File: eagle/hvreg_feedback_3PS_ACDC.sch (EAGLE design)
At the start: 35 parts

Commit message: tweaks - submit to advanced circuits
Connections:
- net N$10: now also U$3.-VOUT
- net N$5: now also U$3.+VOUT
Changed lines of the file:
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@@
 <grid distance="0.1" unitdist="inch" unit="inch" style="lines" multiple="1" display="no" altdistance="0.01" altunitdist="inch" altunit="inch"/>
 <layers>
-<layer number="1" name="Top" color="4" fill="1" visible="yes" active="no"/>
-<layer number="2" name="Route2" color="1" fill="3" visible="yes" active="no"/>
-<layer number="3" name="Route3" color="4" fill="3" visible="yes" active="no"/>
-<layer number="4" name="Route4" color="1" fill="4" visible="yes" active="no"/>
-<layer number="5" name="Route5" color="4" fill="4" visible="yes" active="no"/>
-<layer number="6" name="Route6" color="1" fill="8" visible="yes" active="no"/>
-<layer number="7" name="Route7" color="4" fill="8" visible="yes" active="no"/>
-<layer number="8" name="Route8" color="1" fill="2" visible="yes" active="no"/>
-<layer number="9" name="Route9" color="4" fill="2" visible="yes" active="no"/>
-<layer number="10" name="Route10" color="1" fill="7" visible="yes" active="no"/>
-<layer number="11" name="Route11" color="4" fill="7" visible="yes" active="no"/>
-<layer number="12" name="Route12" color="1" fill="5" visible="yes" active="no"/>
-<layer number="13" name="Route13" color="4" fill="5" visible="yes" active="no"/>
-<layer number="14" name="Route14" color="1" fill="6" visible="yes" active="no"/>
-<layer number="15" name="Route15" color="4" fill="6" visible="yes" active="no"/>
-<layer number="16" name="Bottom" color="1" fill="1" visible="yes" active="no"/>
-<layer number="17" name="Pads" color="2" fill="1" visible="yes" active="no"/>
-<layer number="18" name="Vias" color="2" fill="1" visible="yes" active="no"/>
-<layer number="19" name="Unrouted" color="6" fill="1" visible="yes" active="no"/>
-<layer number="20" name="Dimension" color="15" fill="1" visible="yes" active="no"/>
-<layer number="21" name="tPlace" color="7" fill="1" visible="yes" active="no"/>
-<layer number="22" name="bPlace" color="7" fill="1" visible="yes" active="no"/>
-<layer number="23" name="tOrigins" color="15" fill="1" visible="yes" active="no"/>
-<layer number="24" name="bOrigins" color="15" fill="1" visible="yes" active="no"/>
-<layer number="25" name="tNames" color="7" fill="1" visible="yes" active="no"/>
-<layer number="26" name="bNames" color="7" fill="1" visible="yes" active="no"/>
-<layer number="27" name="tValues" color="7" fill="1" visible="yes" active="no"/>
-<layer number="28" name="bValues" color="7" fill="1" visible="yes" active="no"/>
+<layer number="1" name="Top" color="4" fill="1" visible="no" active="no"/>
+<layer number="2" name="Route2" color="1" fill="3" visible="no" active="no"/>
+<layer number="3" name="Route3" color="4" fill="3" visible="no" active="no"/>
+<layer number="4" name="Route4" color="1" fill="4" visible="no" active="no"/>
+<layer number="5" name="Route5" color="4" fill="4" visible="no" active="no"/>
+<layer number="6" name="Route6" color="1" fill="8" visible="no" active="no"/>
+<layer number="7" name="Route7" color="4" fill="8" visible="no" active="no"/>
+<layer number="8" name="Route8" color="1" fill="2" visible="no" active="no"/>
+<layer number="9" name="Route9" color="4" fill="2" visible="no" active="no"/>
+<layer number="10" name="Route10" color="1" fill="7" visible="no" active="no"/>
+<layer number="11" name="Route11" color="4" fill="7" visible="no" active="no"/>
+<layer number="12" name="Route12" color="1" fill="5" visible="no" active="no"/>
+<layer number="13" name="Route13" color="4" fill="5" visible="no" active="no"/>
+<layer number="14" name="Route14" color="1" fill="6" visible="no" active="no"/>
+<layer number="15" name="Route15" color="4" fill="6" visible="no" active="no"/>
+<layer number="16" name="Bottom" color="1" fill="1" visible="no" active="no"/>
+<layer number="17" name="Pads" color="2" fill="1" visible="no" active="no"/>
+<layer number="18" name="Vias" color="2" fill="1" visible="no" active="no"/>
+<layer number="19" name="Unrouted" color="6" fill="1" visible="no" active="no"/>
+<layer number="20" name="Dimension" color="15" fill="1" visible="no" active="no"/>
+<layer number="21" name="tPlace" color="7" fill="1" visible="no" active="no"/>
+<layer number="22" name="bPlace" color="7" fill="1" visible="no" active="no"/>
+<layer number="23" name="tOrigins" color="15" fill="1" visible="no" active="no"/>
+<layer number="24" name="bOrigins" color="15" fill="1" visible="no" active="no"/>
+<layer number="25" name="tNames" color="7" fill="1" visible="no" active="no"/>
+<layer number="26" name="bNames" color="7" fill="1" visible="no" active="no"/>
+<layer number="27" name="tValues" color="7" fill="1" visible="no" active="no"/>
+<layer number="28" name="bValues" color="7" fill="1" visible="no" active="no"/>
 <layer number="29" name="tStop" color="7" fill="3" visible="no" active="no"/>
 <layer number="30" name="bStop" color="7" fill="6" visible="no" active="no"/>
@@
 <layer number="35" name="tGlue" color="7" fill="4" visible="no" active="no"/>
 <layer number="36" name="bGlue" color="7" fill="5" visible="no" active="no"/>
-<layer number="37" name="tTest" color="7" fill="1" visible="yes" active="no"/>
-<layer number="38" name="bTest" color="7" fill="1" visible="yes" active="no"/>
+<layer number="37" name="tTest" color="7" fill="1" visible="no" active="no"/>
+<layer number="38" name="bTest" color="7" fill="1" visible="no" active="no"/>
 <layer number="39" name="tKeepout" color="4" fill="11" visible="no" active="no"/>
 <layer number="40" name="bKeepout" color="1" fill="11" visible="no" active="no"/>
@@
 <layer number="44" name="Drills" color="7" fill="1" visible="no" active="no"/>
 <layer number="45" name="Holes" color="7" fill="1" visible="no" active="no"/>
-<layer number="46" name="Milling" color="3" fill="1" visible="yes" active="no"/>
-<layer number="47" name="Measures" color="7" fill="1" visible="yes" active="no"/>
-<layer number="48" name="Document" color="7" fill="1" visible="yes" active="no"/>
-<layer number="49" name="Reference" color="7" fill="1" visible="yes" active="no"/>
-<layer number="50" name="dxf" color="7" fill="1" visible="yes" active="no"/>
-<layer number="51" name="tDocu" color="7" fill="1" visible="yes" active="no"/>
-<layer number="52" name="bDocu" color="7" fill="1" visible="yes" active="no"/>
-<layer number="53" name="tGND_GNDA" color="7" fill="9" visible="yes" active="no"/>
-<layer number="54" name="bGND_GNDA" color="1" fill="9" visible="yes" active="no"/>
-<layer number="56" name="wert" color="7" fill="1" visible="yes" active="no"/>
+<layer number="46" name="Milling" color="3" fill="1" visible="no" active="no"/>
+<layer number="47" name="Measures" color="7" fill="1" visible="no" active="no"/>
+<layer number="48" name="Document" color="7" fill="1" visible="no" active="no"/>
+<layer number="49" name="Reference" color="7" fill="1" visible="no" active="no"/>
+<layer number="50" name="dxf" color="7" fill="1" visible="no" active="no"/>
+<layer number="51" name="tDocu" color="7" fill="1" visible="no" active="no"/>
+<layer number="52" name="bDocu" color="7" fill="1" visible="no" active="no"/>
+<layer number="53" name="tGND_GNDA" color="7" fill="9" visible="no" active="no"/>
+<layer number="54" name="bGND_GNDA" color="1" fill="9" visible="no" active="no"/>
+<layer number="56" name="wert" color="7" fill="1" visible="no" active="no"/>
 <layer number="90" name="Modules" color="5" fill="1" visible="yes" active="yes"/>
 <layer number="91" name="Nets" color="2" fill="1" visible="yes" active="yes"/>
@@
 <wire x1="144.78" y1="50.8" x2="144.78" y2="48.26" width="0.1524" layer="91"/>
 <junction x="144.78" y="48.26"/>
+<pinref part="U$3" gate="G$1" pin="+VOUT"/>
 </segment>
 </net>
@@
 <wire x1="144.78" y1="10.16" x2="144.78" y2="22.86" width="0.1524" layer="91"/>
 <pinref part="D4" gate="1" pin="C"/>
-</segment>
-</net>
+<pinref part="U$3" gate="G$1" pin="-VOUT"/>
+</segment>
+</net>

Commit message: use lm317, appropriate opamp resistor selection, ultra gatedriver stacks 4 fets
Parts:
- added C17, C18, C19: .1u, rcl:C-US102-043X133
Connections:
- net GND: now also C17.2, C18.2, C19.2
- net N$13: now also C17.1
- net N$14: now also C19.1
- net N$15: now also C18.1
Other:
- moved on the sheet: CONTROLHV-3
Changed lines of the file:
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@@
 <part name="CONTROLHV" library="con-molex" deviceset="KK-156-4" device=""/>
 <part name="FDBKHV" library="con-molex" deviceset="KK-156-4" device=""/>
+<part name="C17" library="rcl" deviceset="C-US" device="102-043X133" value=".1u"/>
+<part name="C18" library="rcl" deviceset="C-US" device="102-043X133" value=".1u"/>
+<part name="C19" library="rcl" deviceset="C-US" device="102-043X133" value=".1u"/>
+<part name="GND24" library="supply1" deviceset="GND" device=""/>
+<part name="GND29" library="supply1" deviceset="GND" device=""/>
+<part name="GND30" library="supply1" deviceset="GND" device=""/>
 </parts>
 <sheets>
@@
 <instance part="CONTROLHV" gate="-1" x="17.78" y="53.34" rot="R180"/>
 <instance part="CONTROLHV" gate="-2" x="106.68" y="27.94" rot="R180"/>
-<instance part="CONTROLHV" gate="-3" x="33.02" y="-5.08" rot="R180"/>
+<instance part="CONTROLHV" gate="-3" x="17.78" y="-5.08" rot="R180"/>
 <instance part="CONTROLHV" gate="-4" x="5.08" y="33.02" rot="R90"/>
 <instance part="FDBKHV" gate="-1" x="96.52" y="63.5"/>
@@
 <instance part="FDBKHV" gate="-3" x="101.6" y="-20.32"/>
 <instance part="FDBKHV" gate="-4" x="12.7" y="33.02" rot="R90"/>
+<instance part="C17" gate="G$1" x="22.86" y="50.8"/>
+<instance part="C18" gate="G$1" x="22.86" y="-7.62"/>
+<instance part="C19" gate="G$1" x="109.22" y="25.4"/>
+<instance part="GND24" gate="1" x="22.86" y="43.18"/>
+<instance part="GND29" gate="1" x="109.22" y="17.78"/>
+<instance part="GND30" gate="1" x="22.86" y="-15.24"/>
 </instances>
 <busses>
@@
 <pinref part="FDBKHV" gate="-4" pin="S"/>
 <pinref part="GND15" gate="1" pin="GND"/>
+</segment>
+<segment>
+<pinref part="C17" gate="G$1" pin="2"/>
+<pinref part="GND24" gate="1" pin="GND"/>
+</segment>
+<segment>
+<pinref part="C19" gate="G$1" pin="2"/>
+<pinref part="GND29" gate="1" pin="GND"/>
+</segment>
+<segment>
+<pinref part="C18" gate="G$1" pin="2"/>
+<pinref part="GND30" gate="1" pin="GND"/>
 </segment>
 </net>
@@
 <segment>
 <pinref part="U$1" gate="G$1" pin="+VIN"/>
-<wire x1="20.32" y1="53.34" x2="35.56" y2="53.34" width="0.1524" layer="91"/>
+<wire x1="20.32" y1="53.34" x2="22.86" y2="53.34" width="0.1524" layer="91"/>
 <pinref part="CONTROLHV" gate="-1" pin="S"/>
+<pinref part="C17" gate="G$1" pin="1"/>
+<wire x1="22.86" y1="53.34" x2="35.56" y2="53.34" width="0.1524" layer="91"/>
+<junction x="22.86" y="53.34"/>
 </segment>
 </net>
@@
 <wire x1="109.22" y1="27.94" x2="119.38" y2="27.94" width="0.1524" layer="91"/>
 <pinref part="CONTROLHV" gate="-2" pin="S"/>
+<pinref part="C19" gate="G$1" pin="1"/>
+<junction x="109.22" y="27.94"/>
 </segment>
 </net>
@@
 <pinref part="U$2" gate="G$1" pin="+VIN"/>
 <pinref part="CONTROLHV" gate="-3" pin="S"/>
-</segment>
-</net>
+<wire x1="20.32" y1="-5.08" x2="22.86" y2="-5.08" width="0.1524" layer="91"/>
+<pinref part="C18" gate="G$1" pin="1"/>
+<wire x1="22.86" y1="-5.08" x2="35.56" y2="-5.08" width="0.1524" layer="91"/>
+<junction x="22.86" y="-5.08"/>
+</segment>
+</net>

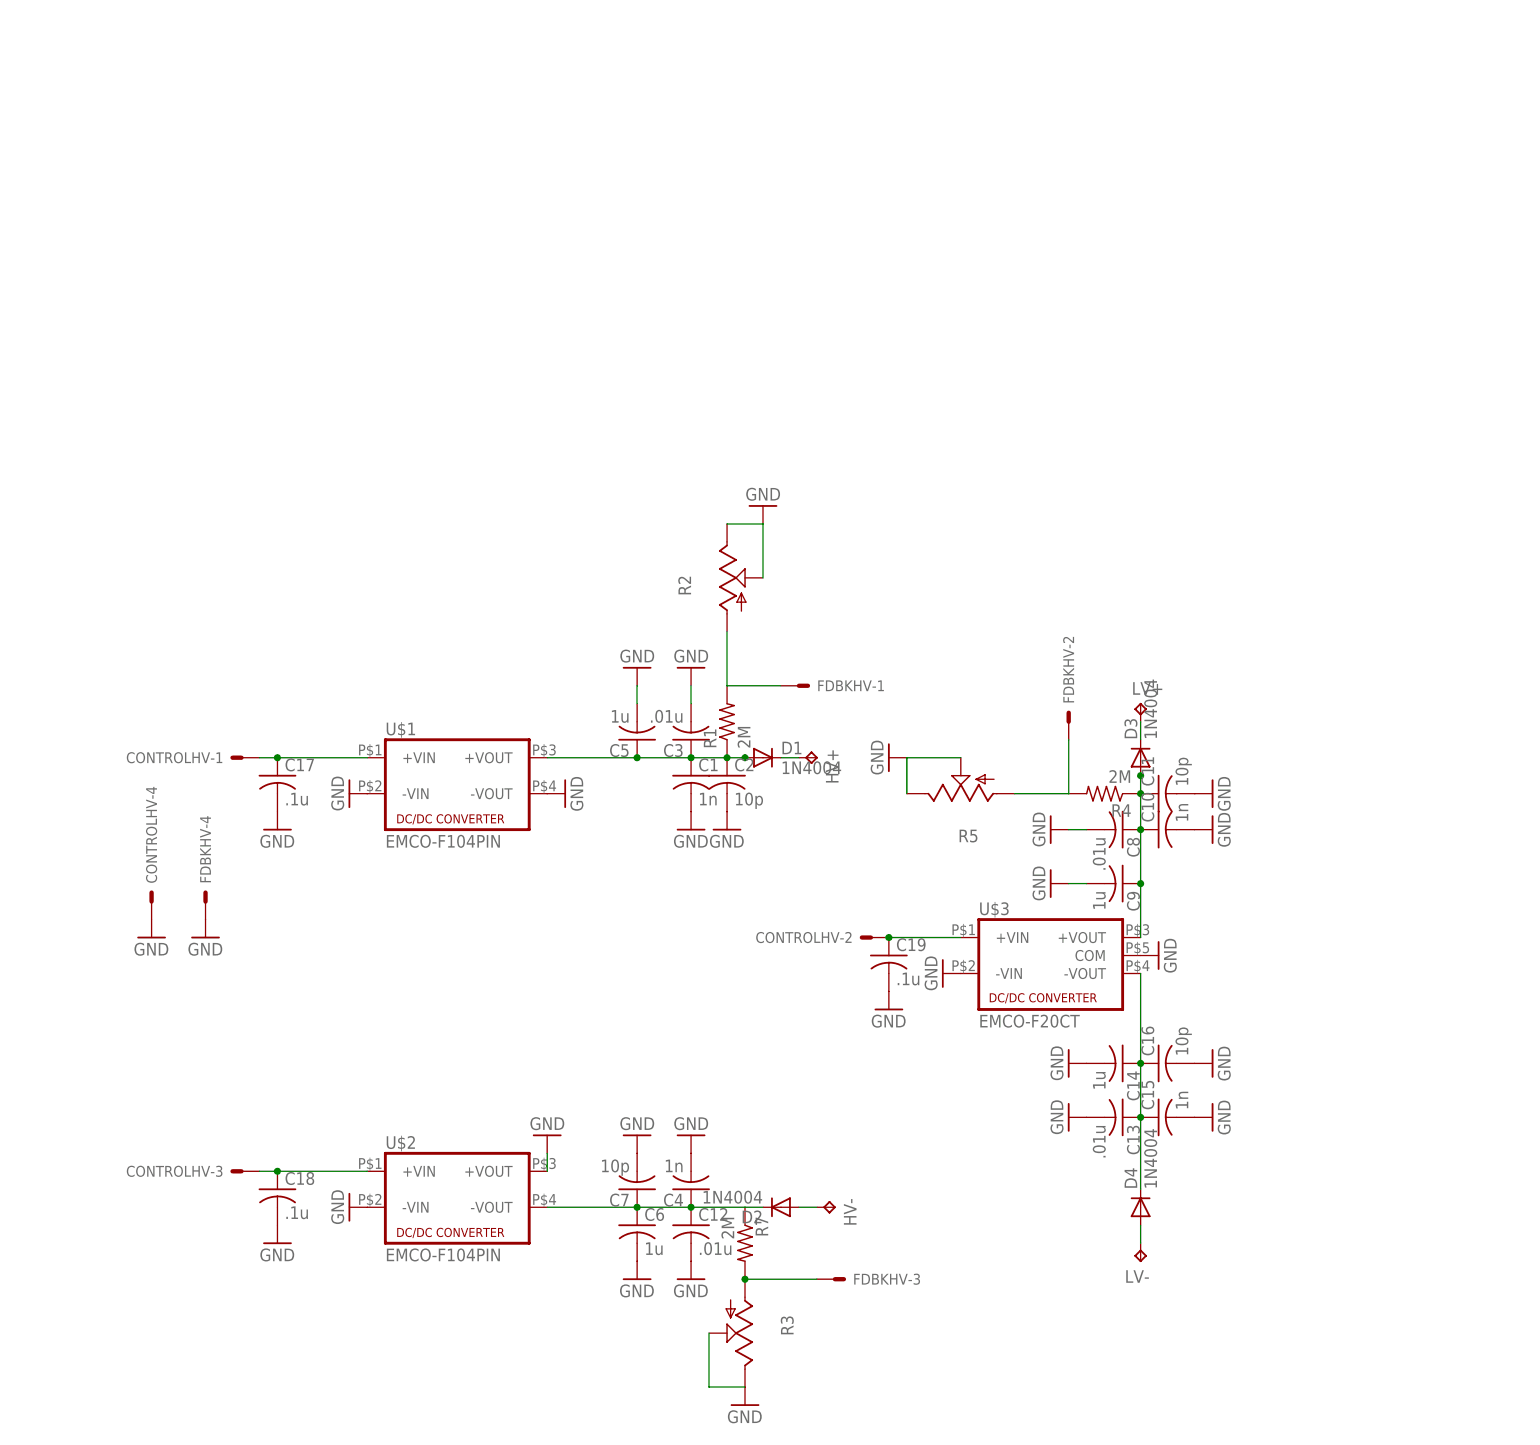
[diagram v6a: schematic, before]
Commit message: optional 317 regulation of emcos
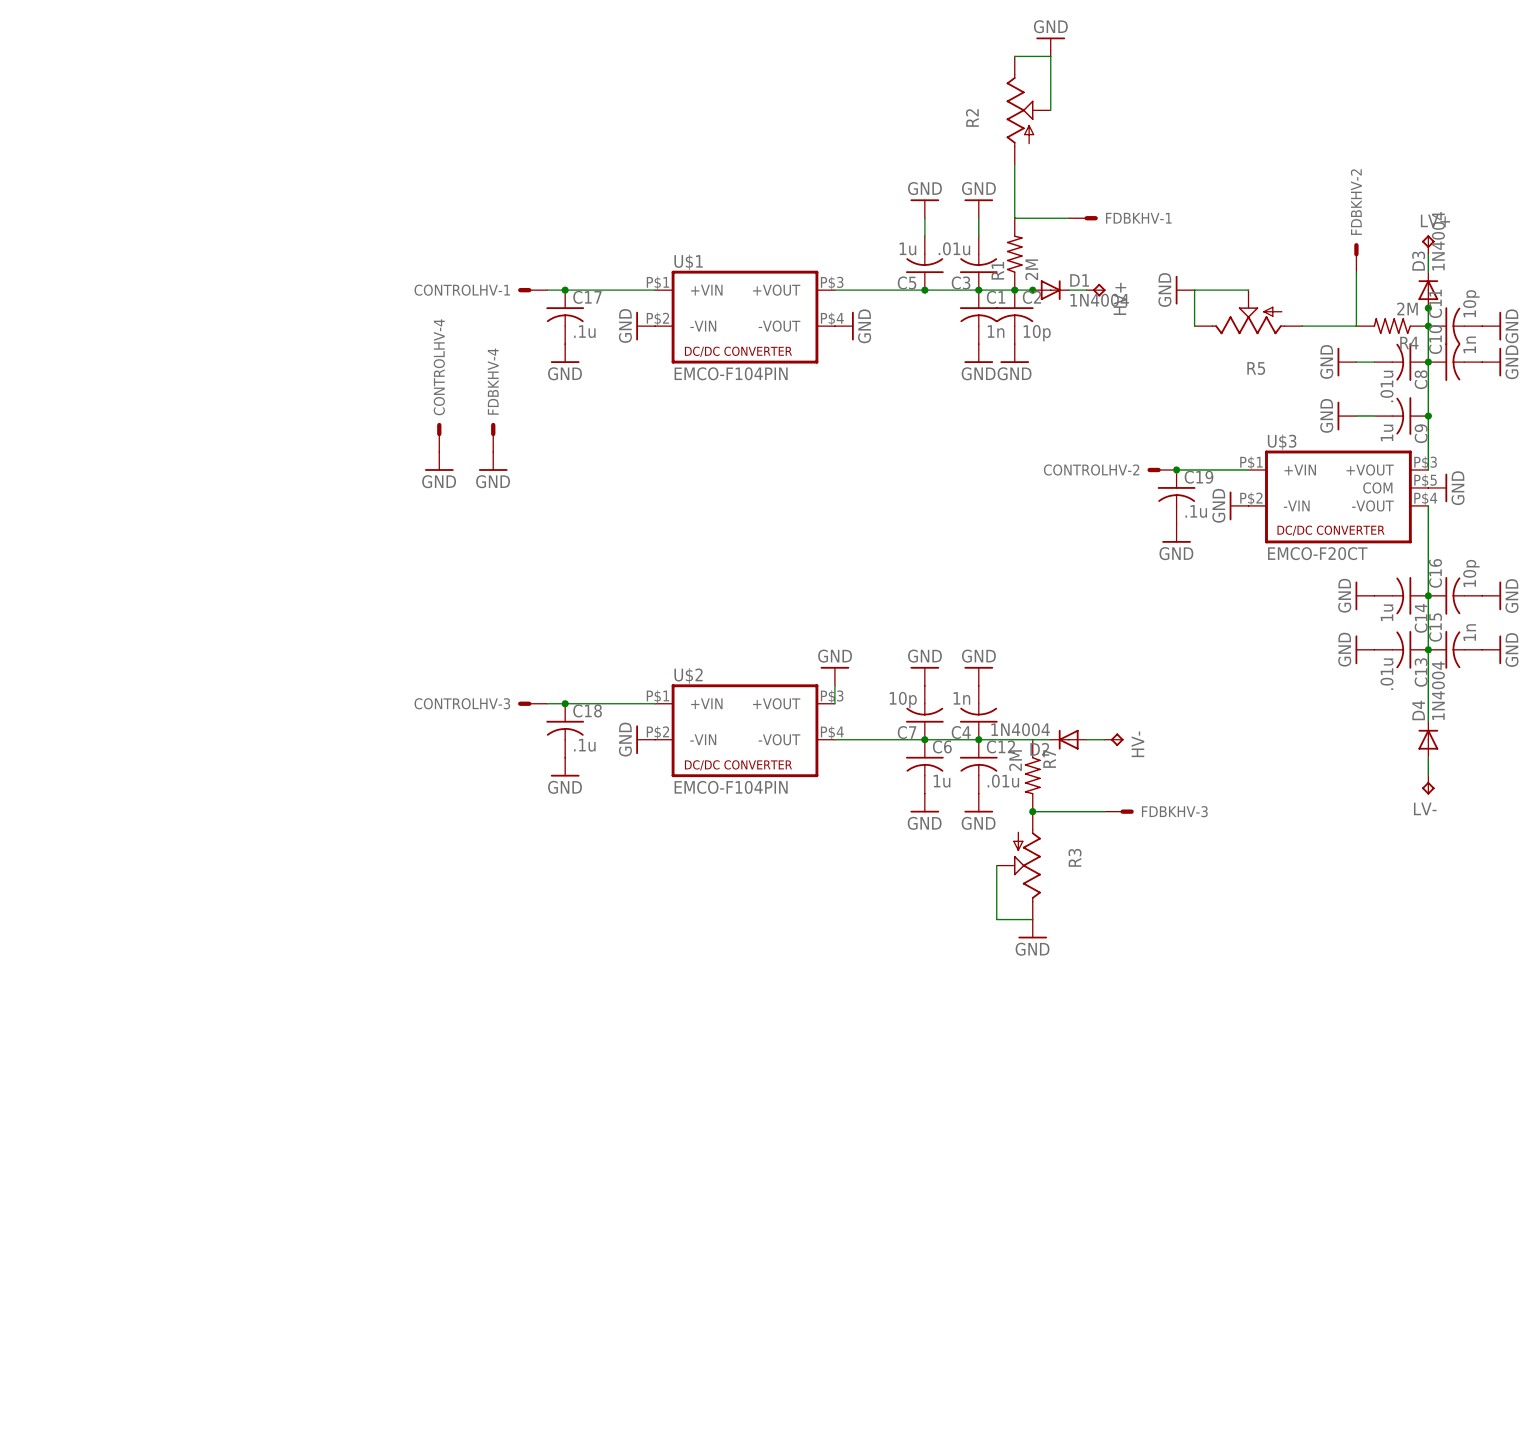
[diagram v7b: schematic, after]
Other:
- moved on the sheet: C1, C10, C11, C12, C13, C14, C15, C16, C17, C18, C19, C2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
